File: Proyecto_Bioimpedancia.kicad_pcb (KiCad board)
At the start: 2 copper layers, 100 x 100 mm, 76 parts, among them J1 Jumper, J2 Jumper, J3 Jumper_Calibration, J4 Jumper, J5 Jumper, J6 Jumper, P1 SD_LAPIZ, P10 UNIVERSAL_PINS, P11 SOURCE_2, P12 RESET, P13 POWER, P14 BIO_OUT1, P15 GND_REGULATOR, P16 BIO_OUT2, P17 TOR_1, P18 TOR_2, P19 TOR_3, P2 GPIO, P20 TOR_4, P3 SOURCE_3, P4 SERIAL_VIRTUAL, P5 ENCODER, P6 I2C, P7 CONN_01X04, P8 SOURCE_1, P9 SPI, SW1 SW_PUSH, U1 AD8606, U2 ADG819, U3 Atmega328PA, U4 LD1117S50TR, Y1 XRCHA_16M

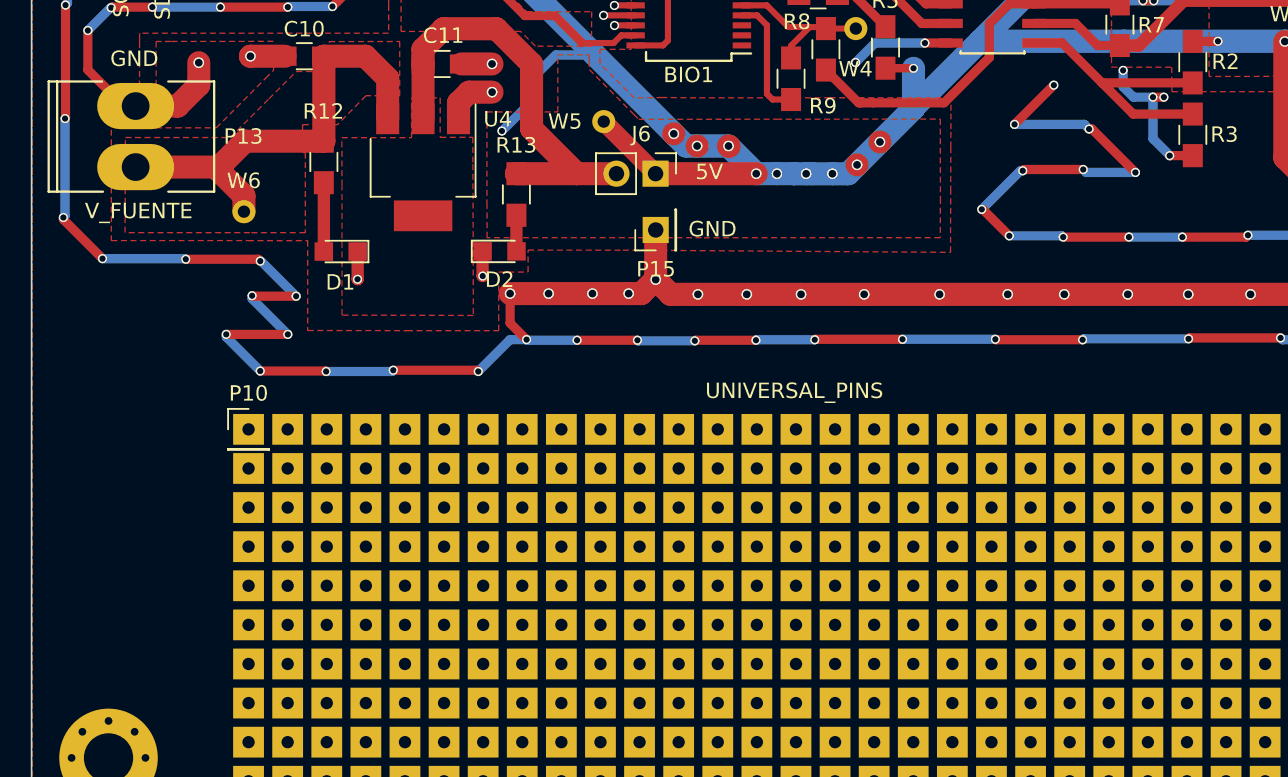
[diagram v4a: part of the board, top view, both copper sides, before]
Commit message: Nombre de Colombia añadido
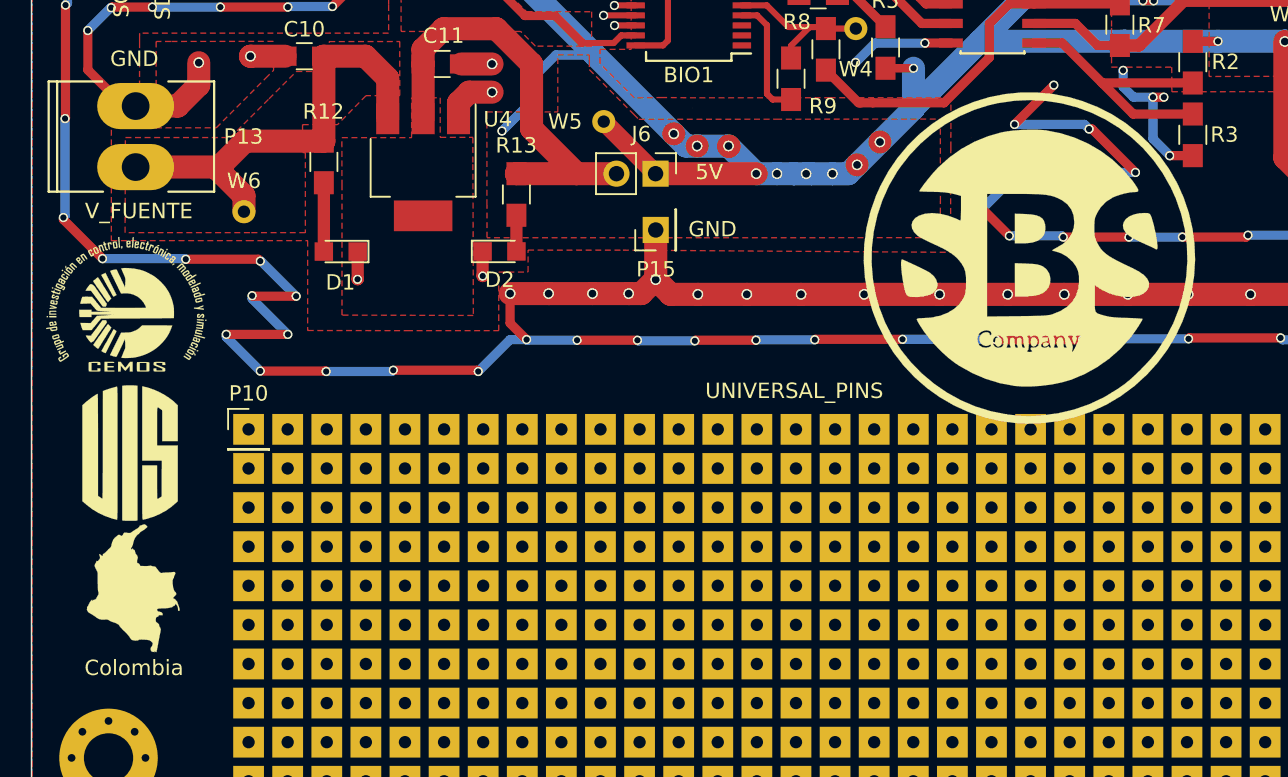
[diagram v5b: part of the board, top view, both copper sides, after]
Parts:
- added G***: LOGO, Logos_Fuentes:SBS_22mm, F.Cu at (151.4, 107.8)
- added G***: LOGO, Logos_Fuentes:CMOS, F.Cu at (92.7, 110.7)
- added G***: LOGO, Logos_Fuentes:UIS, F.Cu at (93.0, 120.4)
- added G***: LOGO, Logos_Fuentes:Colombia, F.Cu at (93.2, 129.3)
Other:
- board text added: "Colombia"
